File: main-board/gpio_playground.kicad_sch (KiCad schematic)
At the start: 28 parts, among them SW4 SW_Push, SW6 SW_Push, SW7 SW_Push, U17 74AHC244, U18 74AHCT1G08, U19 74AHCT1G08, U20 74AHC1G04

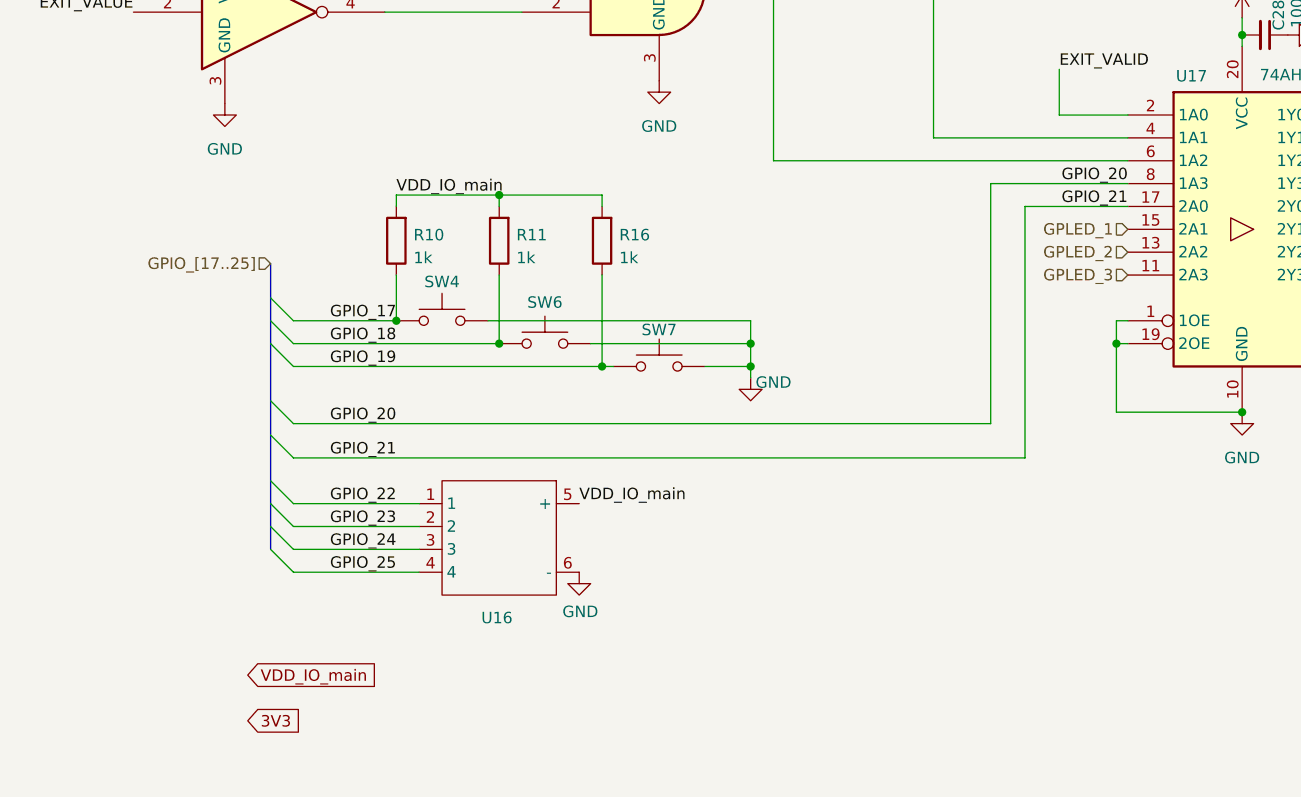
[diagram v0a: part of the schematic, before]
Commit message: Routed all power signals and re-organized GPIOs
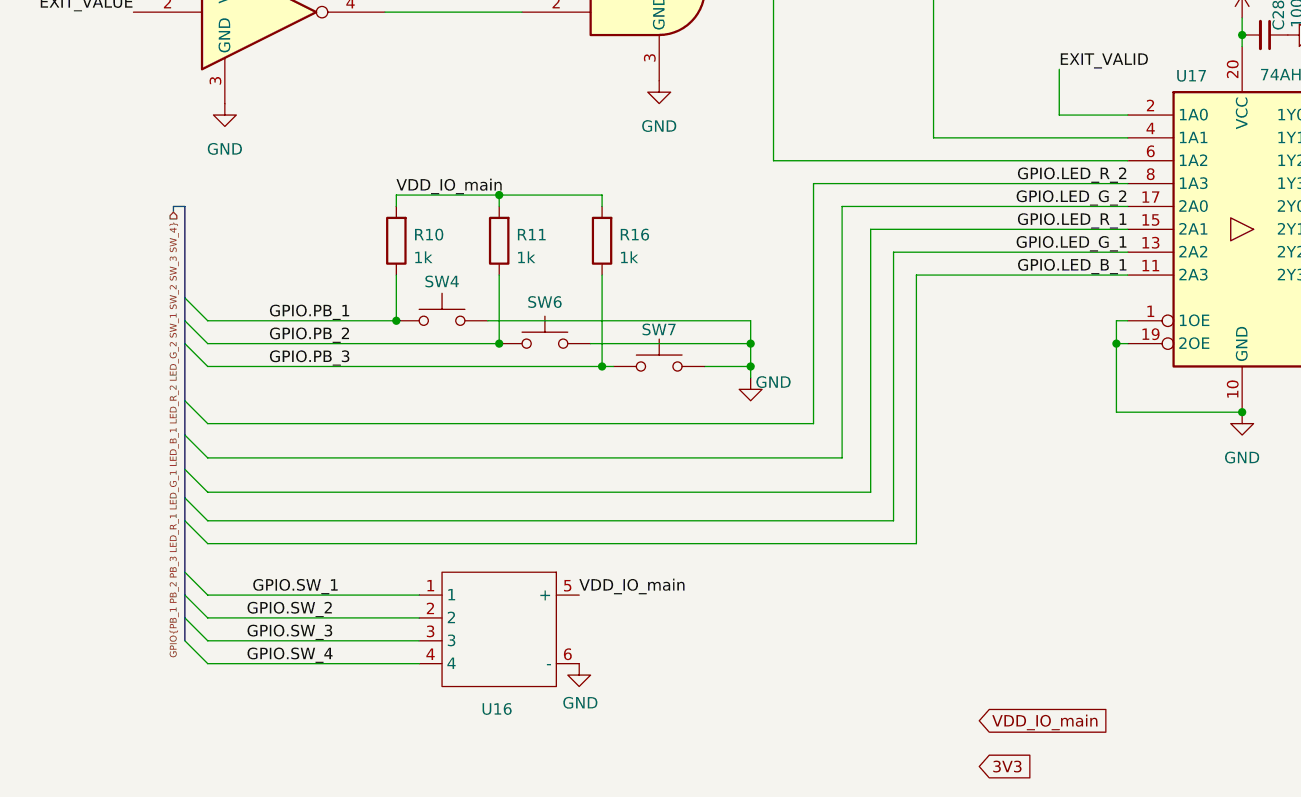
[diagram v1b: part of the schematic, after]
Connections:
- net GPIO_17 renamed GPIO.PB_1
- net GPIO_18 renamed GPIO.PB_2
- net GPIO_19 renamed GPIO.PB_3
- net GPIO_20 renamed GPIO.LED_R_2
- net GPIO_21 renamed GPIO.LED_G_2
- net GPIO_22 renamed GPIO.SW_1
- net GPIO_23 renamed GPIO.SW_2
- net GPIO_24 renamed GPIO.SW_3
- net GPIO_25 renamed GPIO.SW_4
- net GPLED_1 renamed GPIO.LED_R_1
- net GPLED_2 renamed GPIO.LED_G_1
- net GPLED_3 renamed GPIO.LED_B_1
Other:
- moved on the sheet: U16

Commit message: update testing board
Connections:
- net VDD_IO_main renamed VDDIO
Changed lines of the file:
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@@
+		)
+	)
+	(wire
+		(pts
+			(xy 154.94 172.72) (xy 158.75 172.72)
+		)
+		(stroke
+			(width 0)
+			(type default)
 		)
 	)
@@
 	(label "EXIT_VALID"
 		(at 107.95 88.9 180)
+		(effects
+			(font
+				(size 1.27 1.27)
+			)
+			(justify right bottom)
+		)
+	)
+	(label "VDD_IO_main"
+		(at 154.94 172.72 180)
 		(effects
 			(font
@@
 		)
 	)
-	(global_label "VDD_IO_main"
+	(global_label "VDDIO"
 		(shape input)
 		(at 158.75 172.72 0)
@@
 		)
 		(property "Intersheetrefs" "${INTERSHEET_REFS}"
-			(at 173.8304 172.72 0)
+			(at 167.2991 172.72 0)
 			(effects
 				(font

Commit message: pcb update
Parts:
- added R72, R73: 1k, Resistor_SMD:R_0603_1608Metric, symbol Device:R
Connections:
- net GND: now also R73.2; no longer U16.6 (-)
- net VDDIO: now also R72.2; no longer U16.5 (+)
- new net: R73.1, U16.6 (-)
- new net: R72.1, U16.5 (+)
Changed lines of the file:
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@@
+	(wire
+		(pts
+			(xy 116.84 166.37) (xy 114.3 166.37)
+		)
+		(stroke
+			(width 0)
+			(type default)
+		)
+	)
 	(wire
 		(pts
@@
 	(wire
 		(pts
+			(xy 124.46 158.75) (xy 127 158.75)
+		)
+		(stroke
+			(width 0)
+			(type default)
+		)
+	)
+	(wire
+		(pts
 			(xy 73.025 139.7) (xy 140.335 139.7)
 		)
@@
 	(wire
 		(pts
+			(xy 116.84 158.75) (xy 114.3 158.75)
+		)
+		(stroke
+			(width 0)
+			(type default)
+		)
+	)
+	(wire
+		(pts
 			(xy 73.025 128.27) (xy 93.98 128.27)
 		)
@@
 		(pts
 			(xy 149.225 120.65) (xy 175.26 120.65)
+		)
+		(stroke
+			(width 0)
+			(type default)
+		)
+	)
+	(wire
+		(pts
+			(xy 124.46 166.37) (xy 127 166.37)
 		)
 		(stroke
@@
 	)
 	(label "VDD_IO_main"
-		(at 114.3 158.75 0)
+		(at 127 158.75 0)
 		(effects
 			(font
@@
 			)
 			(justify right)
+		)
+	)
+	(symbol
+		(lib_id "Device:R")
+		(at 120.65 166.37 90)
+		(unit 1)
+		(exclude_from_sim no)
+		(in_bom yes)
+		(on_board yes)
+		(dnp no)
+		(property "Reference" "R73"
+			(at 115.57 165.1 90)
+			(effects
+				(font
+					(size 1.27 1.27)
+				)
+			)
+		)
+		(property "Value" "1k"
+			(at 125.095 165.1 90)
+			(effects
+				(font
+					(size 1.27 1.27)
+				)
+			)
+		)
+		(property "Footprint" "Resistor_SMD:R_0603_1608Metric"
+			(at 120.65 168.148 90)
+			(effects
+				(font
+					(size 1.27 1.27)
+				)
+				(hide yes)
+			)
+		)
+		(property "Datasheet" "~"
+			(at 120.65 166.37 0)
+			(effects
+				(font
+					(size 1.27 1.27)
+				)
+				(hide yes)
+			)
+		)
+		(property "Description" ""
+			(at 120.65 166.37 0)
+			(effects
+				(font
+					(size 1.27 1.27)
+				)
+				(hide yes)
+			)
+		)
+		(property "LCSC" "C21190"
+			(at 120.65 161.29 0)
+			(effects
+				(font
+					(size 1.27 1.27)
+				)
+				(hide yes)
+			)
+		)
+		(pin "1"
+		)
+		(pin "2"
+		)
+		(instances
+			(project "main-board"
+				(path "/6198f783-b154-4adf-87fa-b1d9cb913fe2/fd9da62b-9782-45f1-a1dc-4f8db8879f00"
+					(reference "R73")
+					(unit 1)
+				)
+			)
 		)
 	)
@@
 	(symbol
 		(lib_id "power:GND")
-		(at 114.3 166.37 0)
+		(at 127 166.37 0)
 		(unit 1)
 		(exclude_from_sim no)
@@
 		(dnp no)
 		(property "Reference" "#PWR11"
-			(at 114.3 172.72 0)
+			(at 127 172.72 0)
 			(effects
 				(font
@@
 		)
 		(property "Value" "GND"
-			(at 114.427 170.7642 0)
+			(at 127.127 170.7642 0)
 			(effects
 				(font
@@
 		)
 		(property "Footprint" ""
-			(at 114.3 166.37 0)
+			(at 127 166.37 0)
 			(effects
 				(font
@@
 		)
 		(property "Datasheet" ""
-			(at 114.3 166.37 0)
+			(at 127 166.37 0)
 			(effects
 				(font
@@
 		)
 		(property "Description" "Power symbol creates a global label with name \"GND\" , ground"
-			(at 114.3 166.37 0)
+			(at 127 166.37 0)
 			(effects
 				(font
@@
 					(unit 1)
 				)
+			)
+		)
+	)
+	(symbol
+		(lib_id "Device:R")
+		(at 120.65 158.75 90)
+		(unit 1)
+		(exclude_from_sim no)
+		(in_bom yes)
+		(on_board yes)
+		(dnp no)
+		(property "Reference" "R72"
+			(at 115.57 157.48 90)
+			(effects
+				(font
+					(size 1.27 1.27)
+				)
+			)
+		)
+		(property "Value" "1k"
+			(at 125.095 157.48 90)
+			(effects
+				(font
+					(size 1.27 1.27)
+				)
+			)
+		)
+		(property "Footprint" "Resistor_SMD:R_0603_1608Metric"
+			(at 120.65 160.528 90)
+			(effects
+				(font
+					(size 1.27 1.27)
+				)
+				(hide yes)
+			)
+		)
+		(property "Datasheet" "~"
+			(at 120.65 158.75 0)
+			(effects
+				(font
+					(size 1.27 1.27)
+				)
+				(hide yes)
+			)
+		)
+		(property "Description" ""
+			(at 120.65 158.75 0)
+			(effects
+				(font
+					(size 1.27 1.27)
+				)
+				(hide yes)
+			)
+		)
+		(property "LCSC" "C21190"
+			(at 120.65 153.67 0)
+			(effects
+				(font
+					(size 1.27 1.27)
+				)
+				(hide yes)
+			)
+		)
+		(pin "1"
+		)
+		(pin "2"
+		)
+		(instances
+			(project "main-board"
+				(path "/6198f783-b154-4adf-87fa-b1d9cb913fe2/fd9da62b-9782-45f1-a1dc-4f8db8879f00"
+					(reference "R72")
+					(unit 1)
+				)

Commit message: pcb update
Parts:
- added J1: Conn_02x04_Odd_Even, Connector_PinHeader_2.54mm:PinHeader_2x04_P2.54mm_Vertical_SMD, symbol Connector_Generic:Conn_02x04_Odd_Even
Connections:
- net GPIO.SW_1: now also J1.7 (Pin_7); no longer U16.1
- net GPIO.SW_2: now also J1.5 (Pin_5); no longer U16.2
- net GPIO.SW_3: now also J1.3 (Pin_3); no longer U16.3
- net GPIO.SW_4: now also J1.1 (Pin_1); no longer U16.4
- new net: J1.2 (Pin_2), U16.4
- new net: J1.4 (Pin_4), U16.3
- new net: J1.6 (Pin_6), U16.2
- new net: J1.8 (Pin_8), U16.1
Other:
- moved on the sheet: R72, R73, U16
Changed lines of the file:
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@@
 	(wire
 		(pts
-			(xy 116.84 166.37) (xy 114.3 166.37)
+			(xy 130.81 166.37) (xy 128.27 166.37)
 		)
 		(stroke
@@
 	(wire
 		(pts
+			(xy 109.22 166.37) (xy 110.49 166.37)
+		)
+		(stroke
+			(width 0)
+			(type default)
+		)
+	)
+	(wire
+		(pts
 			(xy 213.995 113.03) (xy 210.82 113.03)
 		)
@@
 	(wire
 		(pts
-			(xy 124.46 158.75) (xy 127 158.75)
+			(xy 138.43 158.75) (xy 140.97 158.75)
 		)
 		(stroke
@@
 	(wire
 		(pts
+			(xy 109.22 163.83) (xy 110.49 163.83)
+		)
+		(stroke
+			(width 0)
+			(type default)
+		)
+	)
+	(wire
+		(pts
 			(xy 116.84 114.3) (xy 116.84 115.57)
 		)
@@
 	(wire
 		(pts
-			(xy 116.84 158.75) (xy 114.3 158.75)
+			(xy 130.81 158.75) (xy 128.27 158.75)
 		)
 		(stroke
@@
 	(wire
 		(pts
-			(xy 124.46 166.37) (xy 127 166.37)
+			(xy 138.43 166.37) (xy 140.97 166.37)
 		)
 		(stroke
@@
 	(wire
 		(pts
+			(xy 109.22 158.75) (xy 110.49 158.75)
+		)
+		(stroke
+			(width 0)
+			(type default)
+		)
+	)
+	(wire
+		(pts
 			(xy 105.41 114.3) (xy 116.84 114.3)
 		)
@@
 		)
 	)
+	(wire
+		(pts
+			(xy 109.22 161.29) (xy 110.49 161.29)
+		)
+		(stroke
+			(width 0)
+			(type default)
+		)
+	)
 	(label "GPIO.PB_1"
 		(at 88.9 128.27 180)
@@
 	)
 	(label "VDD_IO_main"
-		(at 127 158.75 0)
+		(at 140.97 158.75 0)
 		(effects
 			(font
@@
 	(symbol
 		(lib_id "Device:R")
-		(at 120.65 166.37 90)
+		(at 134.62 166.37 90)
 		(unit 1)
 		(exclude_from_sim no)
@@
 		(dnp no)
 		(property "Reference" "R73"
-			(at 115.57 165.1 90)
+			(at 129.54 165.1 90)
 			(effects
 				(font
@@
 		)
 		(property "Value" "1k"
-			(at 125.095 165.1 90)
+			(at 139.065 165.1 90)
 			(effects
 				(font
@@
 		)
 		(property "Footprint" "Resistor_SMD:R_0603_1608Metric"
-			(at 120.65 168.148 90)
+			(at 134.62 168.148 90)
 			(effects
 				(font
@@
 		)
 		(property "Datasheet" "~"
-			(at 120.65 166.37 0)
+			(at 134.62 166.37 0)
 			(effects
 				(font
@@
 		)
 		(property "Description" ""
-			(at 120.65 166.37 0)
+			(at 134.62 166.37 0)
 			(effects
 				(font
@@
 		)
 		(property "LCSC" "C21190"
-			(at 120.65 161.29 0)
+			(at 134.62 161.29 0)
 			(effects
 				(font
@@
 	)
 	(symbol
+		(lib_id "Connector_Generic:Conn_02x04_Odd_Even")
+		(at 101.6 163.83 0)
+		(mirror x)
+		(unit 1)
+		(exclude_from_sim no)
+		(in_bom yes)
+		(on_board yes)
+		(dnp no)
+		(property "Reference" "J1"
+			(at 102.87 152.4 0)
+			(effects
+				(font
+					(size 1.27 1.27)
+				)
+			)
+		)
+		(property "Value" "Conn_02x04_Odd_Even"
+			(at 102.87 154.94 0)
+			(effects
+				(font
+					(size 1.27 1.27)
+				)
+			)
+		)
+		(property "Footprint" "Connector_PinHeader_2.54mm:PinHeader_2x04_P2.54mm_Vertical_SMD"
+			(at 101.6 163.83 0)
+			(effects
+				(font
+					(size 1.27 1.27)
+				)
+				(hide yes)
+			)
+		)
+		(property "Datasheet" "~"
+			(at 101.6 163.83 0)
+			(effects
+				(font
+					(size 1.27 1.27)
+				)
+				(hide yes)
+			)
+		)
+		(property "Description" "Generic connector, double row, 02x04, odd/even pin numbering scheme (row 1 odd numbers, row 2 even numbers), script generated (kicad-library-utils/schlib/autogen/connector/)"
+			(at 101.6 163.83 0)
+			(effects
+				(font
+					(size 1.27 1.27)
+				)
+				(hide yes)
+			)
+		)
+		(pin "2"
+		)
+		(pin "7"
+		)
+		(pin "4"
+		)
+		(pin "1"
+		)
+		(pin "5"
+		)
+		(pin "3"
+		)
+		(pin "8"
+		)
+		(pin "6"
+		)
+		(instances
+			(project ""
+				(path "/6198f783-b154-4adf-87fa-b1d9cb913fe2/fd9da62b-9782-45f1-a1dc-4f8db8879f00"
+					(reference "J1")
+					(unit 1)
+				)
+			)
+		)
+	)
+	(symbol
 		(lib_id "Device:R")
 		(at 207.01 118.11 90)
@@
 	(symbol
 		(lib_id "cheeps-tb:SPDT-4bit-tri-state")
-		(at 111.76 168.91 0)
+		(at 125.73 168.91 0)
 		(mirror y)
 		(unit 1)
@@
 		(dnp no)
 		(property "Reference" "U16"
-			(at 105.156 171.45 0)
+			(at 119.126 171.45 0)
 			(effects
 				(font
@@
 		)
 		(property "Value" "~"
-			(at 105.41 154.94 0)
+			(at 119.38 154.94 0)
 			(effects
 				(font
@@
 		)
 		(property "Footprint" "heep_footprints:BIWIN_DTS04GE_SMD"
-			(at 111.76 168.91 0)
+			(at 125.73 168.91 0)
 			(effects
 				(font
@@
 		)
 		(property "Datasheet" "https://www.lcsc.com/datasheet/C3294670.pdf"
-			(at 111.76 168.91 0)
+			(at 125.73 168.91 0)
 			(effects
 				(font
@@
 		)
 		(property "Description" ""
-			(at 111.76 168.91 0)
+			(at 125.73 168.91 0)
 			(effects
 				(font
@@
 	(symbol
 		(lib_id "power:GND")
-		(at 127 166.37 0)
+		(at 140.97 166.37 0)
 		(unit 1)
 		(exclude_from_sim no)
@@
 		(dnp no)
 		(property "Reference" "#PWR11"
-			(at 127 172.72 0)
+			(at 140.97 172.72 0)
 			(effects
 				(font
@@
 		)
 		(property "Value" "GND"
-			(at 127.127 170.7642 0)
+			(at 141.097 170.7642 0)
 			(effects
 				(font
@@
 		)
 		(property "Footprint" ""
-			(at 127 166.37 0)
+			(at 140.97 166.37 0)
 			(effects
 				(font
@@
 		)
 		(property "Datasheet" ""
-			(at 127 166.37 0)
+			(at 140.97 166.37 0)
 			(effects
 				(font
@@
 		)
 		(property "Description" "Power symbol creates a global label with name \"GND\" , ground"
-			(at 127 166.37 0)
+			(at 140.97 166.37 0)
 			(effects
 				(font
@@
 	(symbol
 		(lib_id "Device:R")
-		(at 120.65 158.75 90)
+		(at 134.62 158.75 90)
 		(unit 1)
 		(exclude_from_sim no)
@@
 		(dnp no)
 		(property "Reference" "R72"
-			(at 115.57 157.48 90)
+			(at 129.54 157.48 90)
 			(effects
 				(font
@@
 		)
 		(property "Value" "1k"
-			(at 125.095 157.48 90)
+			(at 139.065 157.48 90)
 			(effects
 				(font
@@
 		)
 		(property "Footprint" "Resistor_SMD:R_0603_1608Metric"
-			(at 120.65 160.528 90)
+			(at 134.62 160.528 90)
 			(effects
 				(font
@@
 		)
 		(property "Datasheet" "~"
-			(at 120.65 158.75 0)
+			(at 134.62 158.75 0)
 			(effects
 				(font
@@
 		)
 		(property "Description" ""
-			(at 120.65 158.75 0)
+			(at 134.62 158.75 0)
 			(effects
 				(font
@@
 		)
 		(property "LCSC" "C21190"
-			(at 120.65 153.67 0)
+			(at 134.62 153.67 0)
 			(effects
 				(font

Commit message: PCB update
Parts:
- C28: value 100n -> 100nF
- D1, D9: LCSC C84263 -> C84266
- D3, D5, D8: LCSC C84263 -> C965804
- J1: LCSC (none) -> C192300
- SW4, SW6, SW7: LCSC (none) -> C221678
- U16: value ~ -> BIWIN_DTS04GE_SMD; LCSC (none) -> C3294670; lcsc (none) -> C3294670
- U17: LCSC (none) -> C7475
- U18, U19: LCSC (none) -> C113521
- U20: LCSC (none) -> C7465
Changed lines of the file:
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@@
+			)
+		)
+		(property "LCSC" "C192300"
+			(at 102.87 152.4 0)
+			(effects
+				(font
+					(size 1.27 1.27)
+				)
+				(hide yes)
 			)
 		)
@@
 		(property "Description" "Push button switch, generic, two pins"
 			(at 110.49 130.81 0)
+			(effects
+				(font
+					(size 1.27 1.27)
+				)
+				(hide yes)
+			)
+		)
+		(property "LCSC" "C221678"
+			(at 110.49 126.238 0)
 			(effects
 				(font
@@
 			)
 		)
+		(property "LCSC" "C7475"
+			(at 180.594 101.092 0)
+			(effects
+				(font
+					(size 1.27 1.27)
+				)
+				(hide yes)
+			)
+		)
 		(pin "1"
 		)
@@
 			)
 		)
-		(property "Value" "~"
+		(property "Value" "BIWIN_DTS04GE_SMD"
 			(at 119.38 154.94 0)
 			(effects
@@
 			)
 		)
+		(property "lcsc" "C3294670"
+			(at 125.73 168.91 0)
+			(effects
+				(font
+					(size 1.27 1.27)
+				)
+				(hide yes)
+			)
+		)
+		(property "LCSC" "C3294670"
+			(at 119.126 171.45 0)
+			(effects
+				(font
+					(size 1.27 1.27)
+				)
+				(hide yes)
+			)
+		)
 		(pin "5"
 		)
@@
 		(property "Description" "Push button switch, generic, two pins"
 			(at 123.19 133.35 0)
+			(effects
+				(font
+					(size 1.27 1.27)
+				)
+				(hide yes)
+			)
+		)
+		(property "LCSC" "C221678"
+			(at 123.19 129.286 0)
 			(effects
 				(font
@@
 			)
 		)
-		(property "LCSC" "C84263"
+		(property "LCSC" "C84266"
 			(at 217.805 123.19 0)
 			(effects
@@
 			)
 		)
-		(property "LCSC" "C84263"
+		(property "LCSC" "C965804"
 			(at 217.805 120.65 0)
 			(effects
@@
 			)
 		)
-		(property "LCSC" "C84263"
+		(property "LCSC" "C965804"
 			(at 217.805 110.49 0)
 			(effects
@@
 			)
 		)
-		(property "LCSC" "C84263"
+		(property "LCSC" "C84266"
 			(at 217.805 105.41 0)
 			(effects
@@
 			)
 		)
+		(property "LCSC" "C113521"
+			(at 135.89 85.1214 0)
+			(effects
+				(font
+					(size 1.27 1.27)
+				)
+				(hide yes)
+			)
+		)
 		(pin "1"
 		)
@@
 		(property "Description" "Push button switch, generic, two pins"
 			(at 99.06 128.27 0)
+			(effects
+				(font
+					(size 1.27 1.27)
+				)
+				(hide yes)
+			)
+		)
+		(property "LCSC" "C221678"
+			(at 99.06 123.952 0)
 			(effects
 				(font
@@
 			)
 		)
+		(property "LCSC" "C113521"
+			(at 147.32 60.9914 0)
+			(effects
+				(font
+					(size 1.27 1.27)
+				)
+				(hide yes)
+			)
+		)
 		(pin "1"
 		)
@@
 			)
 		)
+		(property "LCSC" "C7465"
+			(at 92.71 87.6614 0)
+			(effects
+				(font
+					(size 1.27 1.27)
+				)
+				(hide yes)
+			)
+		)
 		(pin "4"
 		)
@@
 			)
 		)
-		(property "LCSC" "C84263"
+		(property "LCSC" "C965804"
 			(at 217.805 115.57 0)
 			(effects
@@
 			)
 		)
-		(property "Value" "100n"
+		(property "Value" "100nF"
 			(at 194.056 91.313 0)
 			(effects

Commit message: Testing board final version & production data
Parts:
- removed J1: Conn_02x04_Odd_Even, Connector_PinHeader_2.54mm:PinHeader_2x04_P2.54mm_Vertical_SMD, symbol Connector_Generic:Conn_02x04_Odd_Even
- removed R72, R73: 1k, Resistor_SMD:R_0603_1608Metric, symbol Device:R
- added C33: 100nF, Capacitor_SMD:C_0603_1608Metric, symbol Device:C_Small
- added D19, D20, D21, D22, D23, D24, D25, D26: LED, LED_SMD:LED_0603_1608Metric, symbol Device:LED
- added R111, R112, R113, R114, R115, R116, R117, R77, R79, R95: 1k, Resistor_SMD:R_0603_1608Metric, symbol Device:R
- added U11: 74AHC244, Package_SO:TSSOP-20_4.4x6.5mm_P0.65mm, symbol 74xx:74AHC244
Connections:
- net 3V3: now also C33.2, D26.2 (A), U11.20 (VCC)
- net GND: now also C33.1, D19.1 (K), D20.1 (K), D21.1 (K), D22.1 (K), D23.1 (K), D24.1 (K), D25.1 (K), R117.1, U11.1 (1OE), U11.10 (GND), U11.19 (2OE)
- net GPIO.PB_1: now also U11.4 (1A1)
- net GPIO.PB_2: now also U11.6 (1A2)
- net GPIO.PB_3: now also U11.8 (1A3)
- net GPIO.SW_1: now also U16.1, U11.17 (2A0)
- net GPIO.SW_2: now also U16.2, U11.15 (2A1)
- net GPIO.SW_3: now also U16.3, U11.13 (2A2)
- net GPIO.SW_4: now also U16.4, U11.11 (2A3)
- net VDDIO: now also R116.1
- net at U16.6 (-): now also R117.2
- net at U16.5 (+): now also R116.2
- new net: R79.1, U11.14 (1Y2)
- new net: D19.2 (A), R79.2
- new net: D22.2 (A), R112.2
- new net: R95.1, U11.12 (1Y3)
- new net: R77.1, U11.16 (1Y1)
- new net: R111.1, U11.18 (1Y0)
- new net: R112.1, U11.3 (2Y0)
- new net: R113.1, U11.5 (2Y1)
- new net: R114.1, U11.7 (2Y2)
- new net: R115.1, U11.9 (2Y3)
- new net: D21.2 (A), R95.2
- new net: D20.2 (A), R77.2
- new net: D23.2 (A), R113.2
- new net: D24.2 (A), R114.2
- new net: D25.2 (A), R115.2
- new net: D26.1 (K), R111.2
- new net HEEP_RESET: U11.2 (1A0)
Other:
- moved on the sheet: U16

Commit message: production files
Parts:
- D1, D9: LCSC C84266 -> C84263
- D3, D5, D8: LCSC C965804 -> C84263
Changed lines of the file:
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@@
 			)
 		)
-		(property "LCSC" "C84266"
+		(property "LCSC" "C84263"
 			(at 217.805 123.19 0)
 			(effects
@@
 			)
 		)
-		(property "LCSC" "C965804"
+		(property "LCSC" "C84263"
 			(at 217.805 120.65 0)
 			(effects
@@
 			)
 		)
-		(property "LCSC" "C965804"
+		(property "LCSC" "C84263"
 			(at 217.805 110.49 0)
 			(effects
@@
 			)
 		)
-		(property "LCSC" "C84266"
+		(property "LCSC" "C84263"
 			(at 217.805 105.41 0)
 			(effects
@@
 			)
 		)
-		(property "LCSC" "C965804"
+		(property "LCSC" "C84263"
 			(at 217.805 115.57 0)
 			(effects
